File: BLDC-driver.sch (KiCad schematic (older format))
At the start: 106 parts, among them J1 Conn_01x06, J2 Conn_01x06, J3 Conn_01x02, J4 Encoder, Q1 FDMS8018, Q2 FDMS8018, Q3 FDMS8018, Q4 FDMS8018, Q5 FDMS8018, Q6 FDMS8018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

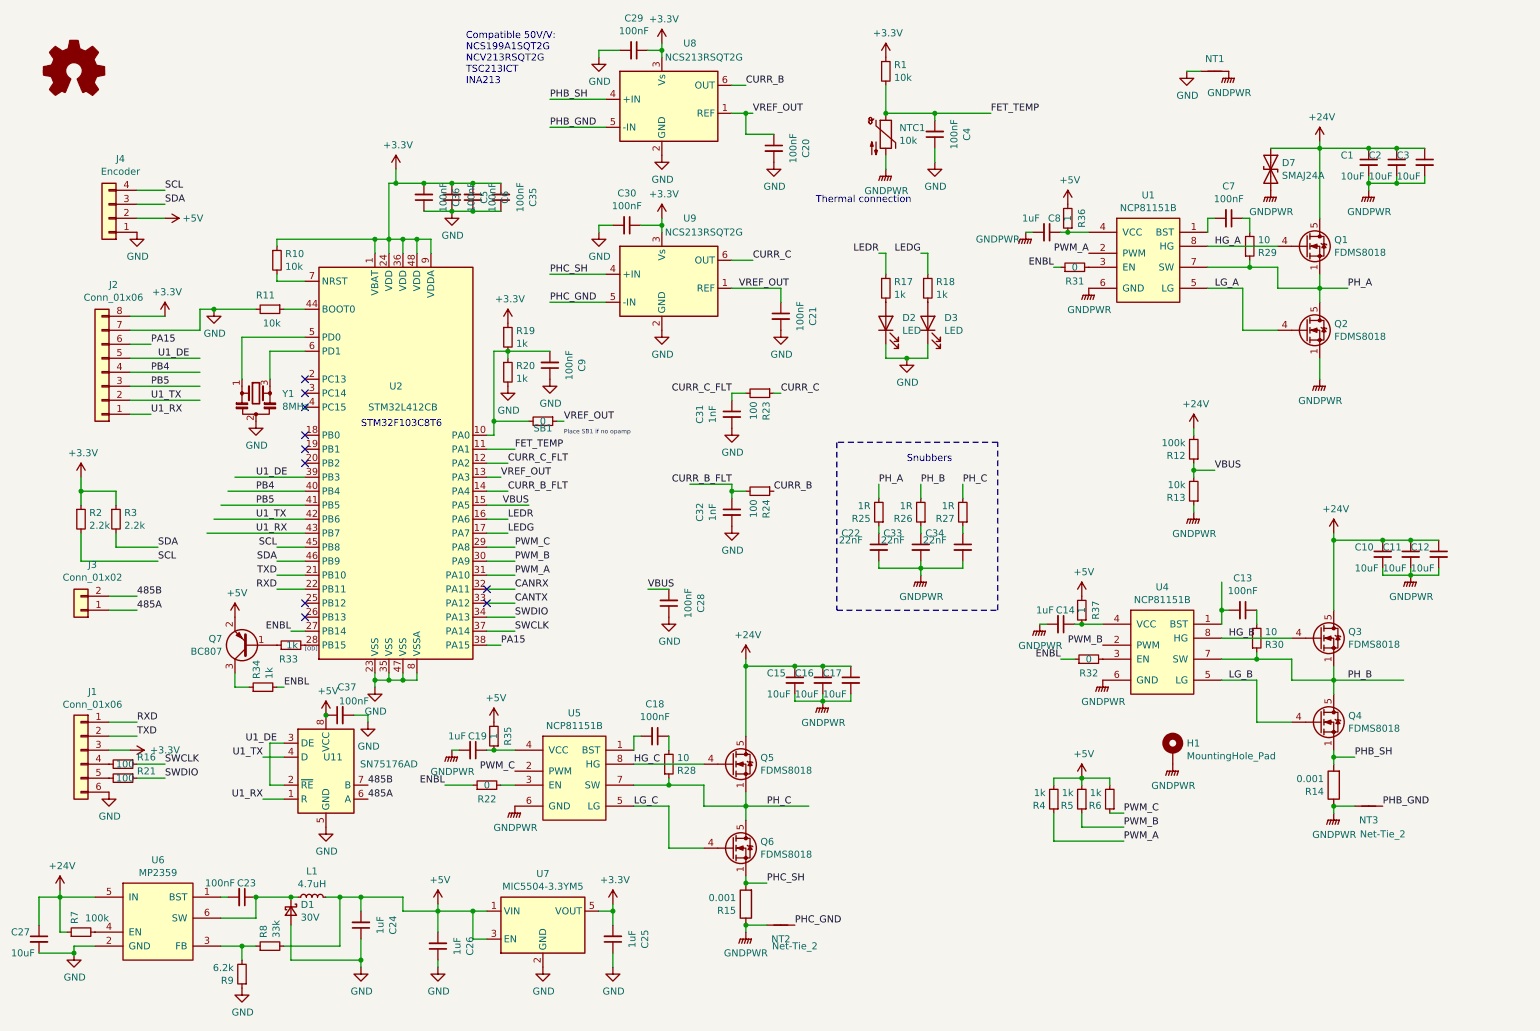
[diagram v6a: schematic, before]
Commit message: Update BOM, change crystal to 16Mhz
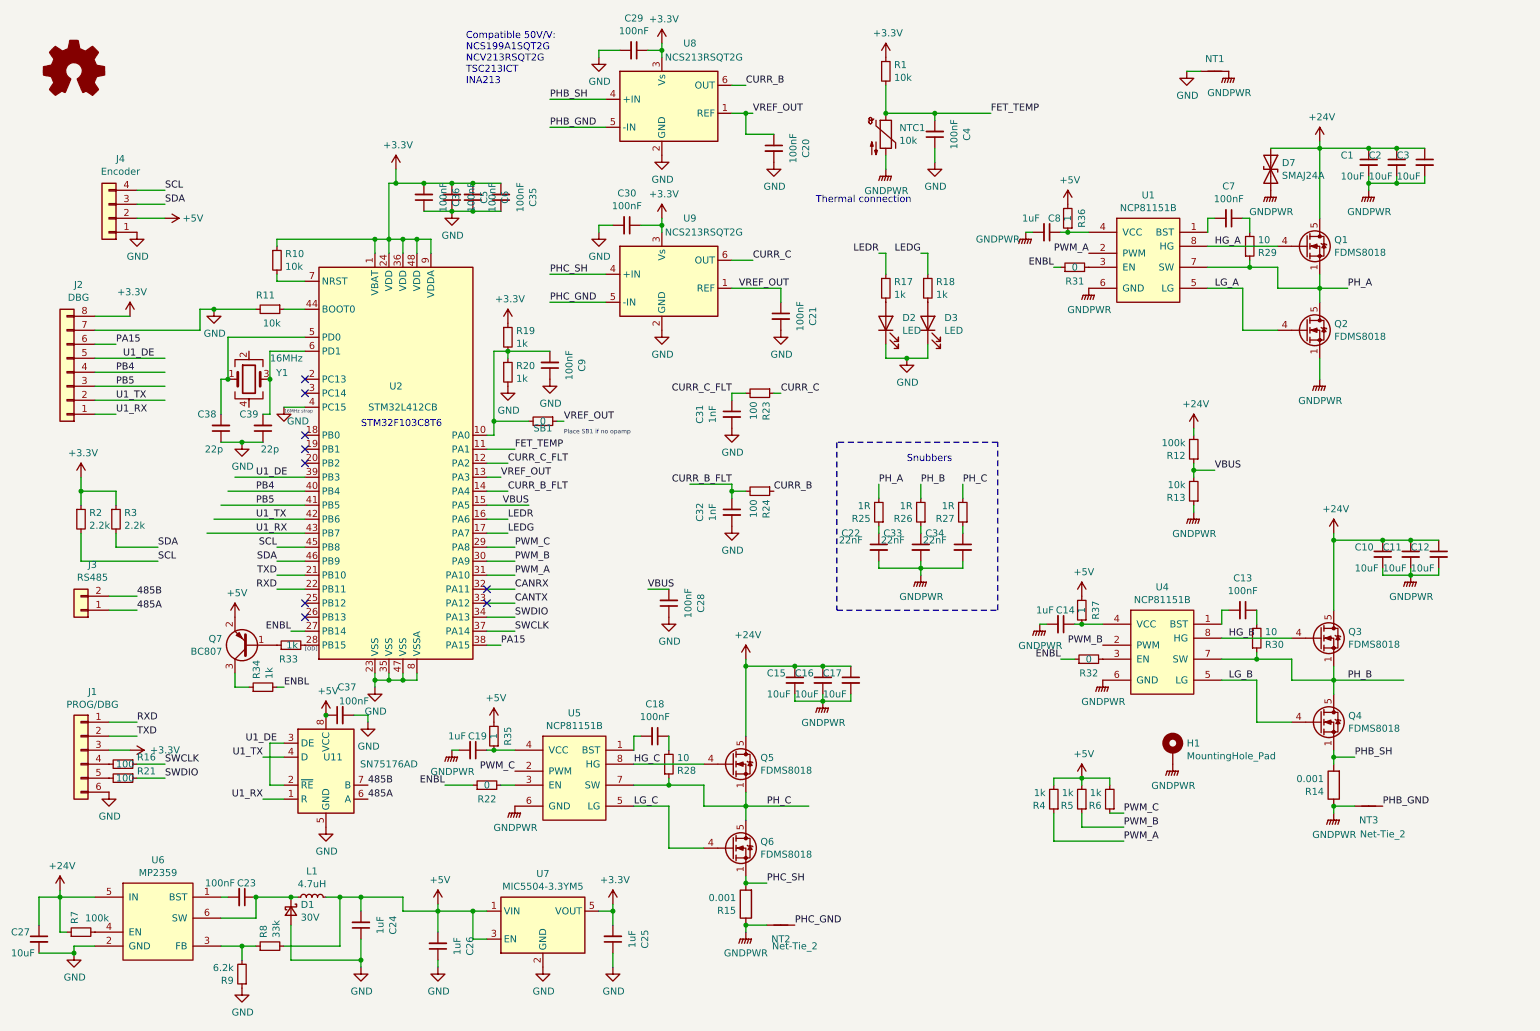
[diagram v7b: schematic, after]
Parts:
- removed Y1: 8MHz, Crystal:Resonator_SMD_muRata_CSTxExxV-3Pin_3.0x1.1mm, symbol Device:Resonator_Small
- added C38, C39: 22p, Capacitor_SMD:C_0402_1005Metric, symbol Device:C_Small
- added Y1: 16MHz, Crystal:Crystal_SMD_3225-4Pin_3.2x2.5mm, symbol Device:Crystal_GND24
- C1, C10, C11, C12, C15, C16, C17, C2, C27, C3: Description (none) -> [Basic] 10uF ±10% 50V X5R 1206 Multilayer Ceramic Capacitor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; MFR (none) -> Samsung Electro-Mechanics; MPN (none) -> CL31A106KBHNNNE
- C13, C18, C20, C21, C23, C28, C29, C30, C35, C36, C37, C4, C5, C6, C7, C9: Description (none) -> [Basic] 100nF ±10% 16V X7R 0402 Multilayer Ceramic Capacito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; MFR (none) -> Samsung Electro-Mechanics; MPN (none) -> CL05B104KO5NNNC
- C14, C19, C24, C8: Description (none) -> [Basic] 1uF ±10% 25V X5R 0402 Multilayer Ceramic Capacitors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; MFR (none) -> Samsung Electro-Mechanics; MPN (none) -> CL05A105KA5NQNC
- C22, C33, C34: Description (none) -> [Basic] Multilayer Ceramic Capacitors MLCC - SMD/SMT 22nF 5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; MFR (none) -> Guangdong Fenghua Advanced Tech; MPN (none) -> 0402B223K500NT
- C25, C26: Description (none) -> [Basic] 1uF ±10% 50V X5R 0603 Multilayer Ceramic Capacitors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; MFR (none) -> Samsung Electro-Mechanics; MPN (none) -> CL10A105KB8NNNC
- C31, C32: Description (none) -> [Basic] 1nF ±10% 50V X7R 0402 Multilayer Ceramic Capacitors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; MFR (none) -> FH(Guangdong Fenghua Advanced Tech); MPN (none) -> 0402B102K500NT
- D2: Description (none) -> LED, RED, 0603; JLCSMT_PKG LED_0603 -> 0603; MFR (none) -> Hubei KENTO Elec; MPN (none) -> KT-0603R
- D3: Description (none) -> [Basic] Green 520~535nm 0603 Light Emitting Diodes (LED) Ro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; MFR (none) -> Everlight Elec; MPN (none) -> 19-217/GHC-YR1S2/3T
- D7: Description (none) -> [Extended] Unidirectional 24V 26.7V 38.9V 10.3A SMA(DO-214A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; JLCSMT (none) -> C10769; JLCSMT_PKG (none) -> SMA,DO-214AC; MFR (none) -> RUILON(Shenzhen Ruilongyuan Elec); MPN SMAJ24A-E3/61 -> SMAJ24A
- J1: value Conn_01x06 -> PROG/DBG
- J2: value Conn_01x06 -> DBG
- J3: value Conn_01x02 -> RS485
- L1: Description (none) -> [Extended] 4.7uH ±20% 1.3A 196mΩ SMD,3x3x1.2mm Power Induct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; JLCSMT (none) -> C305275; JLCSMT_PKG (none) -> SMD,3x3x1.2mm; MFR (none) -> Sunlord; MPN (none) -> WPN3012HS4R7MT
- NTC1: Description (none) -> Thermistor, NTC, 10 kohm, NCU Series, 3380 K, SMD, 0603 [16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; JLCSMT (none) -> C13564; JLCSMT_PKG (none) -> RES-SMD; MFR (none) -> MURATA; SKU (none) -> 2614207; SPR (none) -> Farnell
- Q7: Description (none) -> [Basic] PNP 600mA 150V 300mW SOT-23(SOT-23-3) Bipolar Trans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; MFR (none) -> Changjiang Electronics Tech (CJ); MPN (none) -> MMBT5401
- R1, R10, R11, R13: Description (none) -> [Basic] 10kΩ ±1% 1/16W ±100ppm/℃ 0402 Chip Resistor - Surfa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; MFR (none) -> UNI-ROYAL(Uniroyal Elec); MPN (none) -> 0402WGF1002TCE
- R12, R7: Description (none) -> [Basic] 100kΩ ±1% 1/16W ±100ppm/℃ 0402 Chip Resistor - Surf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; MFR (none) -> UNI-ROYAL(Uniroyal Elec); MPN (none) -> 0402WGF1003TCE
- R14, R15: Description (none) -> [Extended] 0.001Ω ±1% 1W ±75ppm/℃ 1206 Current Sense Resist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; MFR (none) -> RALEC; MPN PMR25HZPFV1L00 -> LR1206-21R001F4
- R16, R21, R23, R24: Description (none) -> [Basic] 100Ω ±1% 1/16W ±200ppm/℃ 0402 Chip Resistor - Surfa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; MFR (none) -> UNI-ROYAL(Uniroyal Elec); MPN (none) -> 0402WGF1000TCE
- R17, R18: Description (none) -> [Basic] 1kΩ ±1% 0.1W ±100ppm/℃ 0603 Chip Resistor - Surface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; MFR (none) -> UNI-ROYAL(Uniroyal Elec); MPN (none) -> 0603WAF1001T5E
- R19, R20, R33, R34, R4, R5, R6: Description (none) -> [Basic] 1kΩ ±1% 1/16W ±100ppm/℃ 0402 Chip Resistor - Surfac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; MFR (none) -> UNI-ROYAL(Uniroyal Elec); MPN (none) -> 0402WGF1001TCE
- R2, R3: Description (none) -> [Basic] Chip Resistor - Surface Mount 2.2KOhms ±1% 1/10W 06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; MFR (none) -> Uniroyal Elec; MPN (none) -> 0603WAF2201T5E
- R22, R31, R32: Description (none) -> [Basic] 0Ω ±1% 0.1W 0603 Chip Resistor - Surface Mount RoHS; MFR (none) -> UNI-ROYAL(Uniroyal Elec); MPN (none) -> 0603WAF0000T5E
- R25, R26, R27, R35, R36, R37: Description (none) -> [Basic] 1Ω ±1% 1/16W ±400ppm/℃ 0402 Chip Resistor - Surface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; MFR (none) -> UNI-ROYAL(Uniroyal Elec); MPN (none) -> 0402WGF100KTCE
- R28, R29, R30: Description (none) -> [Basic] Chip Resistor - Surface Mount 10Ohms ±1% 1/16W 0402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; MFR (none) -> Uniroyal Elec; MPN (none) -> 0402WGF100JTCE
- R8: Description (none) -> [Basic] 33kΩ ±1% 0.1W ±100ppm/℃ 0603 Chip Resistor - Surfac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; MFR (none) -> UNI-ROYAL(Uniroyal Elec); MPN (none) -> 0603WAF3302T5E
- R9: Description (none) -> [Basic] 6.2kΩ ±1% 0.1W ±100ppm/℃ 0603 Chip Resistor - Surfa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; MFR (none) -> UNI-ROYAL(Uniroyal Elec); MPN (none) -> 0603WAF6201T5E
- SB1: Description (none) -> [Basic] 0Ω ±1% 1/16W ±800ppm/℃ 0402 Chip Resistor - Surface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; MFR (none) -> UNI-ROYAL(Uniroyal Elec); MPN (none) -> 0402WGF0000TCE
- U11: Description (none) -> [Basic] Transceiver RS485 1/1 SOIC-8_150mil RS-485/RS-422 I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; MFR (none) -> Texas Instruments; MPN (none) -> SN75176BDR
- U6: Description (none) -> [Extended] TSOT-23-6 DC-DC Converters RoHS; MFR (none) -> Monolithic Power Systems; MPN (none) -> MP2359DJ-LF-Z
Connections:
- wire segments 322 -> 328
- no-connect marks 10 -> 9
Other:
- note added: "16MHz strap"
- moved on the sheet: J2

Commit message: Add encoder FFC connector, change NCP drivers to JLC sourceable
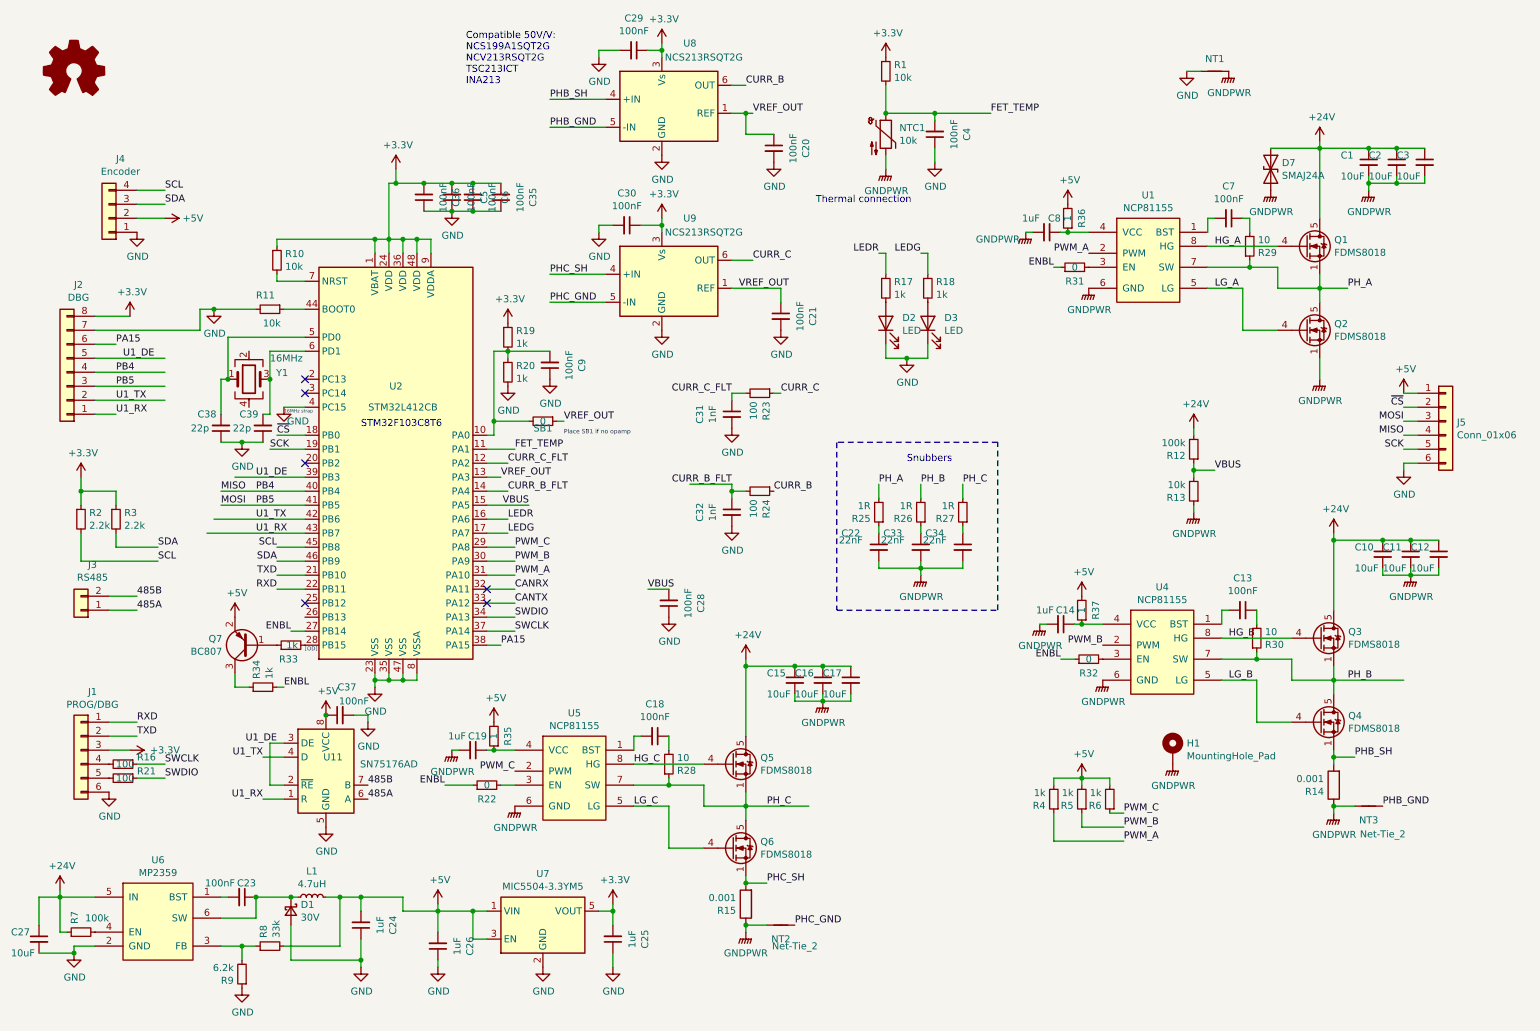
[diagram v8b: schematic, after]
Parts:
- added J5: Conn_01x06, BLDC-Servo:FPC-SMD_F0502-B-06-10G-R, symbol Connector_Generic:Conn_01x06
- U1, U4, U5: value NCP81151B -> NCP81155; footprint Package_DFN_QFN:DFN-8-1EP_2x2mm_P0.5mm_EP0.9x1.5mm -> Package_DFN_QFN:DFN-8-1EP_3x3mm_P0.5mm_EP1.66x2.38mm
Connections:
- net labels added: MISO, MOSI, SCK, ~CS
- wire segments 328 -> 337
- no-connect marks 9 -> 6
